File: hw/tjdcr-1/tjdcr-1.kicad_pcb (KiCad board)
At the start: 4 copper layers, 100 x 35 mm, 72 parts, among them J1 Conn_Coaxial, J2 Tuning, J3 Power, J4 LO Option, J5 Volume, J6 Speaker, Q1 MMBT3904, Q2 MMBFJ310, Q3 MMBT3904, Q4 MMBT3904, Q5 2N3904, T1 5:28, T2 28:5, T3 Transformer_1P_2S, T4 Transformer_1P_2S, T5 42TL013-RC

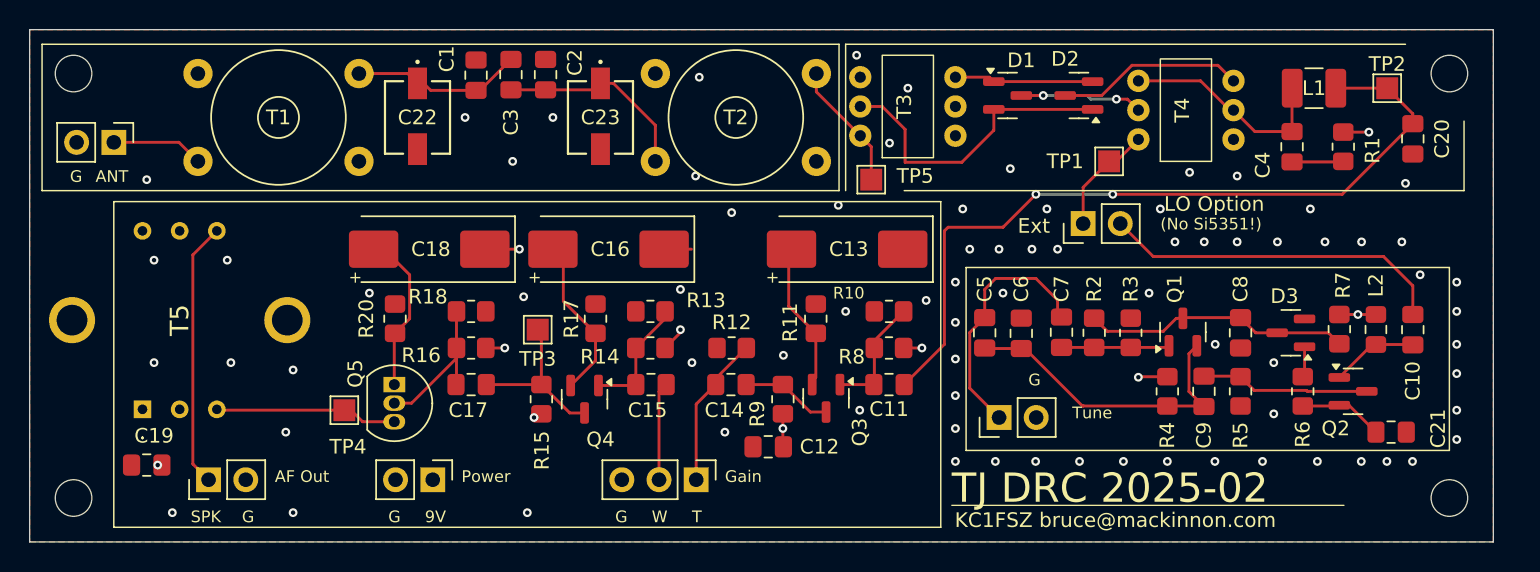
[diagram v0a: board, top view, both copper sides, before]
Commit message: Changed reference numbers
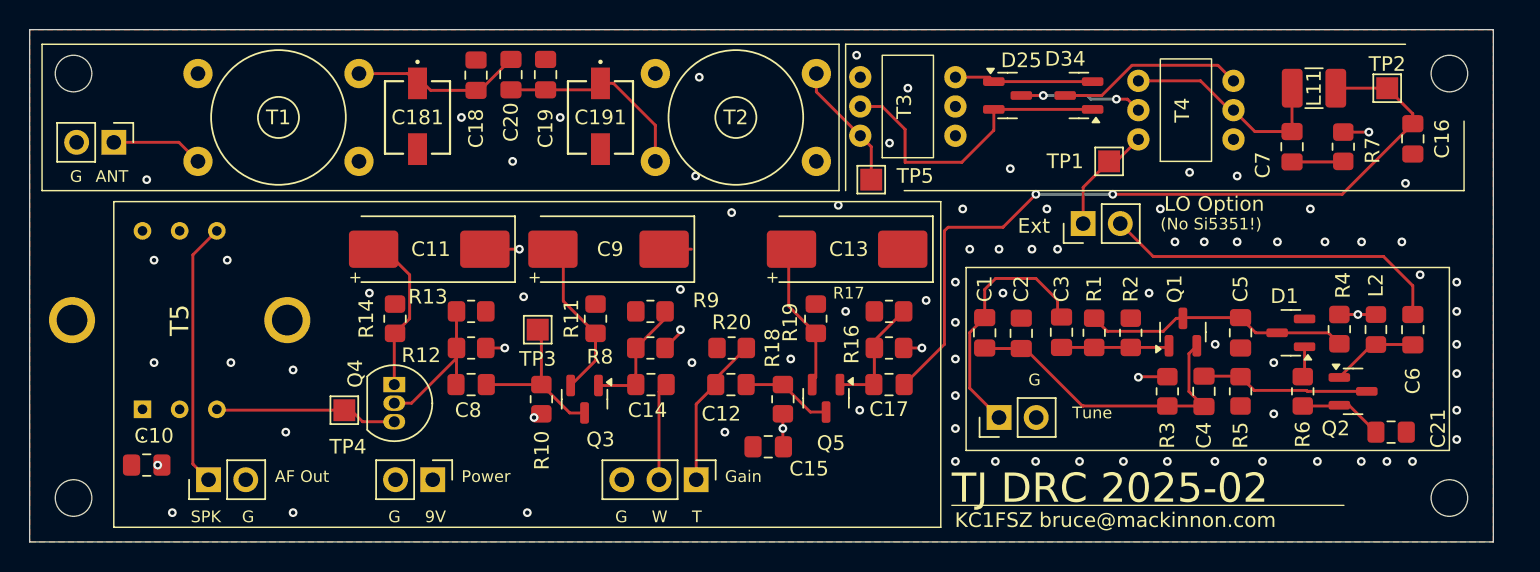
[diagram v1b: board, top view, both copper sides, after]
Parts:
- D1: renamed from D3; value BZX84Cxx -> 8.2V BZX84Cxx (BZX84C8V2LT1G)
- renumbered C5 to C1, C19 to C10, C18 to C11, C14 to C12, C15 to C14, C12 to C15, C20 to C16, C11 to C17, C1 to C18, C22 to C181, C2 to C19, C23 to C191, C6 to C2, C3 to C20, C7 to C3, C9 to C4, C8 to C5, C10 to C6, C4 to C7, C17 to C8, C16 to C9, D1 to D25, D2 to D34, L1 to L11, Q4 to Q3, Q5 to Q4, Q3 to Q5, R2 to R1, R15 to R10, R17 to R11, R16 to R12, R18 to R13, R20 to R14, R8 to R16, R10 to R17, R9 to R18, R11 to R19, R3 to R2, R12 to R20, R4 to R3, R7 to R4, R1 to R7, R14 to R8, R13 to R9

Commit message: Changed reference numbers
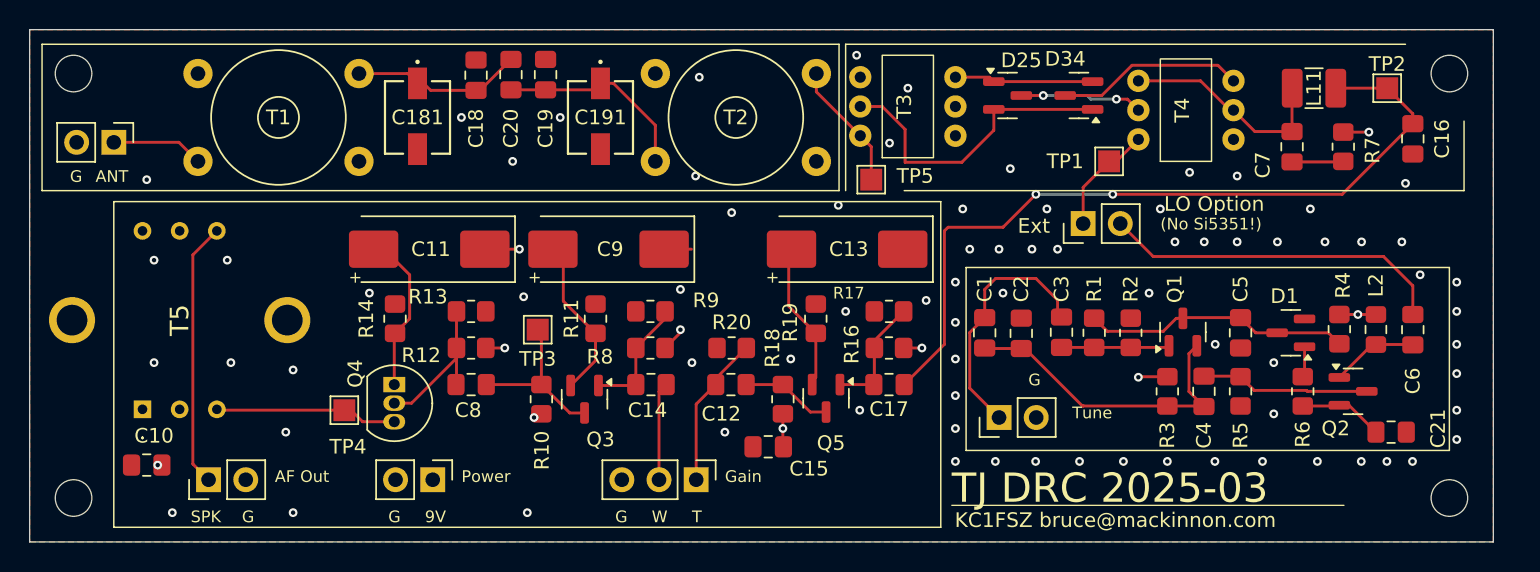
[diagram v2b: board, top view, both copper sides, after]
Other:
- board text added: "TJ DRC 2025-03"
- board text removed: "TJ DRC 2025-02"
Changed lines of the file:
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@@
 		(tags "capacitor handsolder")
 		(property "Reference" "C20"
-			(at 3.25 0 90)
+			(at 3.6765 0 90)
 			(layer "F.SilkS")
 			(effects
@@
 		)
 	)
-	(gr_text "TJ DRC 2025-02"
+	(gr_text "TJ DRC 2025-03"
 		(at 137 83.5 0)
 		(layer "F.SilkS")

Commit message: PCB for 2025-03 board
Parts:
- added C40: C_Variable, bruce-footprints:VCAP_GKG30086-05_SGM-L, F.Cu at (147.5, 79.6)
- added C41: 0.1u, Capacitor_SMD:C_0805_2012Metric_Pad1.18x1.45mm_HandSolder, F.Cu at (156.9, 82.8)
- added J7: TX Offset, Connector_PinHeader_2.54mm:PinHeader_1x02_P2.54mm_Vertical, F.Cu at (163.7, 81.6)
- added Q40: MMBT3904, Package_TO_SOT_SMD:SOT-23, F.Cu at (152.8, 81.8)
- added R40: 47k, Resistor_SMD:R_0805_2012Metric_Pad1.20x1.40mm_HandSolder, F.Cu at (140.7, 76.2)
- added R41: 2.2k, Resistor_SMD:R_0805_2012Metric_Pad1.20x1.40mm_HandSolder, F.Cu at (156.9, 80.8)
- J1: value Conn_Coaxial -> Antenna (50 ohms)
- T3: value Transformer_1P_2S -> Trifilar Toroid
- T4: value Transformer_1P_2S -> Trifiliar Toroid
- moved J2 4.25 mm to (140.3, 81.8)
- moved C9 1.78 mm to (115.4, 66.0), turned to 0 degrees
- moved C1 0.86 mm to (140.1, 71.7)
- moved C2 0.86 mm to (142.6, 71.8)
- moved C3 0.86 mm to (145.4, 71.7)
- moved C4 0.86 mm to (155.1, 75.7)
- moved C5 0.86 mm to (157.6, 71.7)
- moved C6 0.86 mm to (169.4, 71.5)
- moved D1 0.86 mm to (161.0, 71.7)
- moved L2 0.86 mm to (166.8, 71.5)
- moved Q2 0.86 mm to (165.3, 75.7)
- moved R1 0.86 mm to (147.6, 71.7)
- moved R2 0.86 mm to (150.1, 71.7)
- moved R3 0.86 mm to (152.6, 75.7)
- moved R4 0.86 mm to (164.3, 71.5)
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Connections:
- net Net-(D1-K) renamed VREG
- net Net-(Q1-E) renamed OFFSET_A
- C11 pad 1: GND -> Net-(Q4-E)
- C11 pad 2: Net-(Q4-E) -> GND
- C13 pad 1: GND -> Net-(Q5-E)
- C13 pad 2: Net-(Q5-E) -> GND
- C9 pad 1: GND -> Net-(Q3-E)
- C9 pad 2: Net-(Q3-E) -> GND
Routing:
- net Net-(Q40-C): track 0.00 -> 14.3 mm
- net VREG: track 18.3 -> 31.2 mm
- net Net-(J2-Pin_1): track 17.1 -> 24.0 mm
- net Net-(J7-Pin_1): track 0.00 -> 6.15 mm
- net Net-(Q40-B): track 0.00 -> 4.19 mm
- net GND: track 11.4 -> 9.01 mm, vias 80 -> 69
- net LO_O: track 23.7 -> 24.6 mm
- net Net-(Q3-E): track 10.9 -> 11.5 mm
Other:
- board text added: "A"
- board text added: "B"
- board text added: "Shift"
- board text added: "TJDCR 2025-03"
- board text removed: "(No Si5351!)"
- board text removed: "Ext"
- board text removed: "TJ DRC 2025-03"

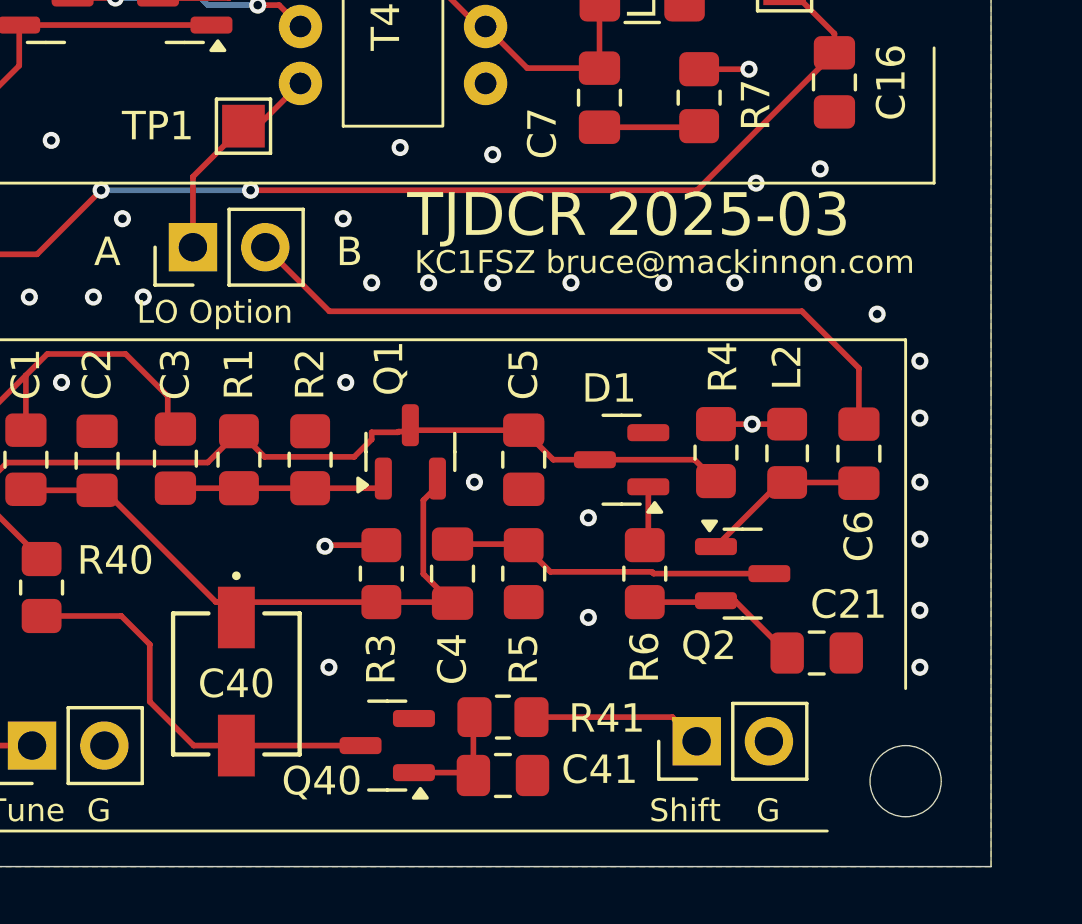
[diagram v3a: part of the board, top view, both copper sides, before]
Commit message: Added BOM to documentation, testing 2025-03 board
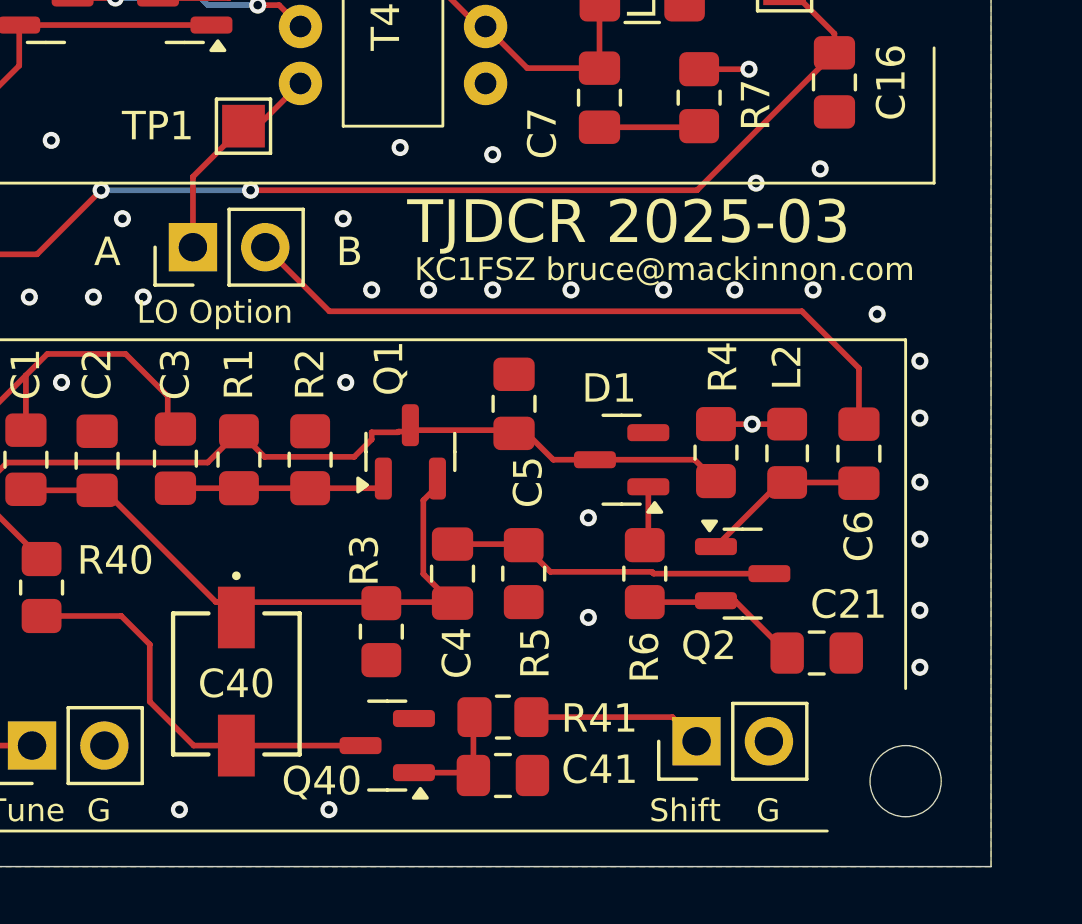
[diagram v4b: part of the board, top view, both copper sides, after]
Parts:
- moved R3 2.04 mm to (152.6, 77.8), turned to -90 degrees
- moved C5 1.99 mm to (157.2, 69.8), turned to 90 degrees
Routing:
- net GND: track 9.01 -> 7.01 mm, vias 69 -> 68
